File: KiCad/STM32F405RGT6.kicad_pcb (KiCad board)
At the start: 4 copper layers, 101.6 x 101.6 mm, 45 parts, among them J1 USB_C_Receptacle_USB2.0, J201 Conn_02x32_Odd_Even, J202 Conn_02x20_Odd_Even, U1 STM32F405RGTx, U2 AT24CS64-SSHM, Y1 25MHz

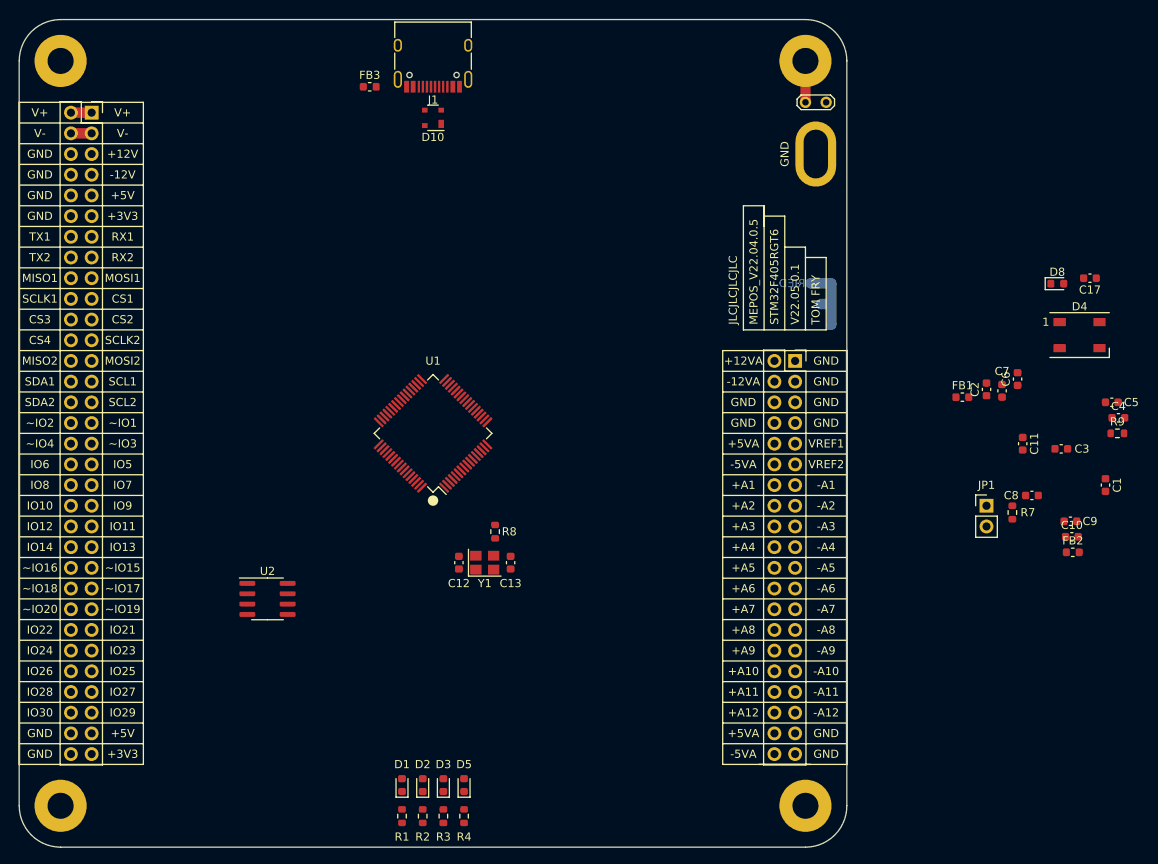
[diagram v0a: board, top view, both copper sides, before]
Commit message: Removed FTDI chip and rearranged pinout
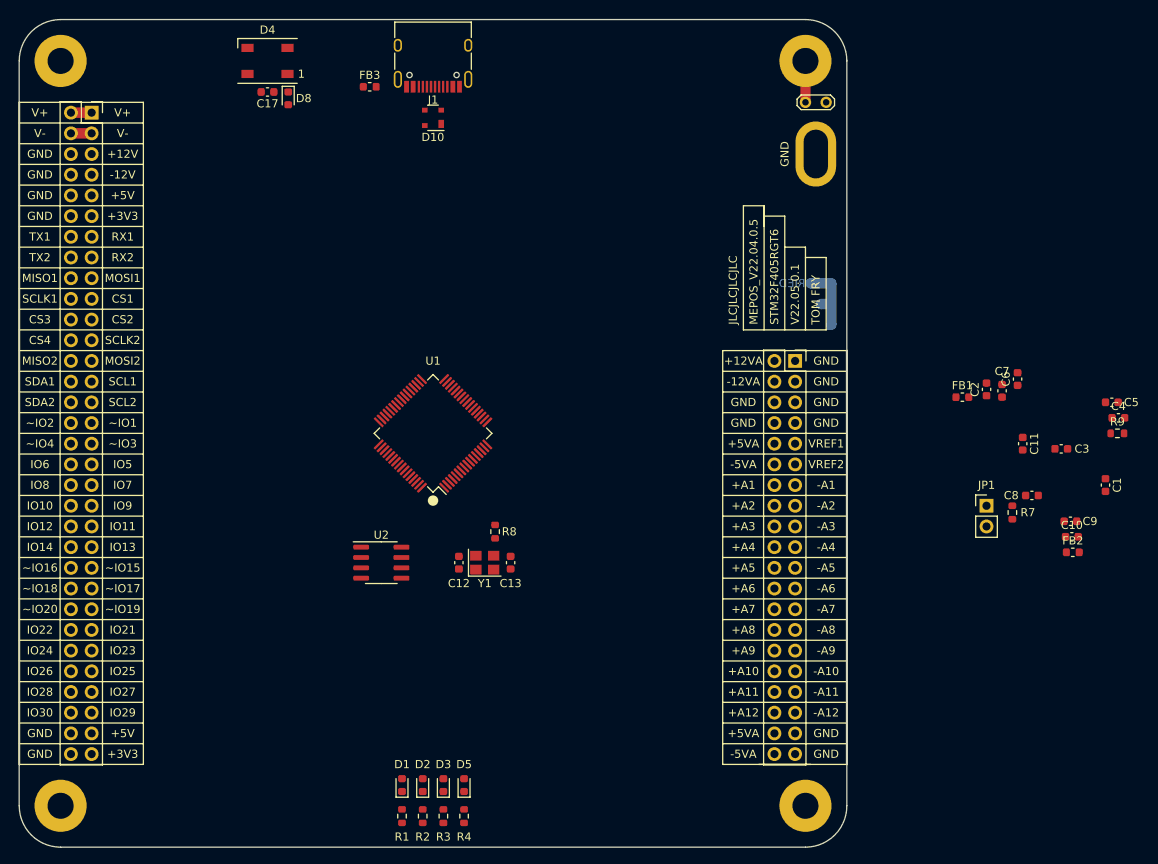
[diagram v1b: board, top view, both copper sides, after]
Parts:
- U2: value AT24CS64-SSHM -> M24C02-RMN
- moved D4 105.2 mm to (124.6, 39.0), turned to 180 degrees
- moved C17 103.5 mm to (124.6, 42.9)
- moved D8 97.1 mm to (127.1, 43.6), turned to -90 degrees
- moved U2 14.7 mm to (138.6, 100.6)

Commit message: Updated Schematic to STM32 software
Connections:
- net FTDI_RST renamed NRST
- U1 pad 2: GPIO10 -> GPIO12
- U1 pad 22: GPIO13 -> GPIO15~
- U1 pad 23: GPIO14 -> GPIO16~
- U1 pad 24: GPIO15~ -> GPIO17~
- U1 pad 25: GPIO16~ -> GPIO18~
- U1 pad 26: GPIO17~ -> GPIO19~
- U1 pad 27: GPIO18~ -> GPIO20~
- U1 pad 3: GPIO11 -> GPIO13
- U1 pad 33: GPIO19~ -> GPIO21
- U1 pad 34: GPIO20~ -> GPIO22
- U1 pad 4: GPIO12 -> GPIO14
- U1 pad 42: FTDI_RX -> TX1
- U1 pad 43: FTDI_TX -> RX1
- U1 pad 44: FTDI_RTS -> GPIO6
- U1 pad 45: FTDI_CTS -> GPIO7
- U1 pad 50: GPIO6 -> GPIO8
- U1 pad 57: GPIO7 -> GPIO9
- U1 pad 58: GPIO8 -> GPIO10
- U1 pad 59: GPIO9 -> GPIO11

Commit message: Updated Schematic and BOM
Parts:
- removed D10: PRTR5V0U2X, Package_TO_SOT_SMD:SOT-143
- added C14: 10uF, Capacitor_SMD:C_0603_1608Metric, F.Cu at (158.8, 46.7)
- added C15: 10uF, Capacitor_SMD:C_0603_1608Metric, F.Cu at (158.8, 44.1)
- added D6: 1N5819WS, Diode_SMD:D_SOD-323, F.Cu at (142.4, 125.0)
- added D7: 1N5819WS, Diode_SMD:D_SOD-323, F.Cu at (155.7, 43.9)
- added D9: 1N5819WS, Diode_SMD:D_SOD-323, F.Cu at (162.7, 49.8)
- added J2: Conn_02x05_Odd_Even, Connector_PinHeader_2.54mm:PinHeader_2x05_P2.54mm_Vertical, F.Cu at (150.0, 129.2)
- added U3: AMS1117-3.3, Package_TO_SOT_SMD:SOT-223-3_TabPin2, F.Cu at (165.2, 44.4)
- added U4: SRV05-4, Package_TO_SOT_SMD:SOT-23-6, F.Cu at (148.7, 46.7)
- moved D1 110.8 mm to (204.6, 37.1)
- moved D2 110.8 mm to (207.2, 37.1)
- moved D3 110.8 mm to (209.7, 37.1)
- moved D5 110.8 mm to (212.2, 37.1)
- moved R1 110.8 mm to (204.6, 40.9)
- moved R2 110.8 mm to (207.2, 40.9)
- moved R3 110.8 mm to (209.7, 40.9)
- moved R4 110.8 mm to (212.2, 40.9)
- moved FB3 15.4 mm to (152.5, 42.9), turned to 180 degrees
- moved J1 0.63 mm to (144.9, 38.8)

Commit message: Updated PCB and Schematic
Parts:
- added C16: 100nF, Capacitor_SMD:C_0603_1608Metric, F.Cu at (167.1, 130.5)
- added SW1: TS-1187A, Button_Switch_SMD:SW_SPST_SKQG_WithStem, F.Cu at (155.1, 130.5)
- added SW2: TS-1187A, Button_Switch_SMD:SW_SPST_SKQG_WithStem, F.Cu at (172.9, 130.5)
- moved R1 114.9 mm to (136.0, 133.2)
- moved R2 114.9 mm to (138.6, 133.2)
- moved R3 114.9 mm to (141.1, 133.2)
- moved R4 114.9 mm to (143.7, 133.2)
- moved D1 113.8 mm to (136.0, 127.9)
- moved D2 113.8 mm to (138.6, 127.9)
- moved D3 113.8 mm to (141.1, 127.9)
- moved D5 113.8 mm to (143.7, 127.9)
- moved C5 97.4 mm to (130.9, 84.8), turned to 90 degrees
- moved C1 88.0 mm to (148.7, 130.5), turned to 90 degrees
- moved C4 83.2 mm to (146.2, 75.2)
- moved C6 82.1 mm to (134.8, 82.9)
- moved C3 79.5 mm to (143.0, 94.9), turned to -90 degrees
- moved R9 79.4 mm to (150.0, 76.5)
- moved R7 77.7 mm to (139.8, 109.5)
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
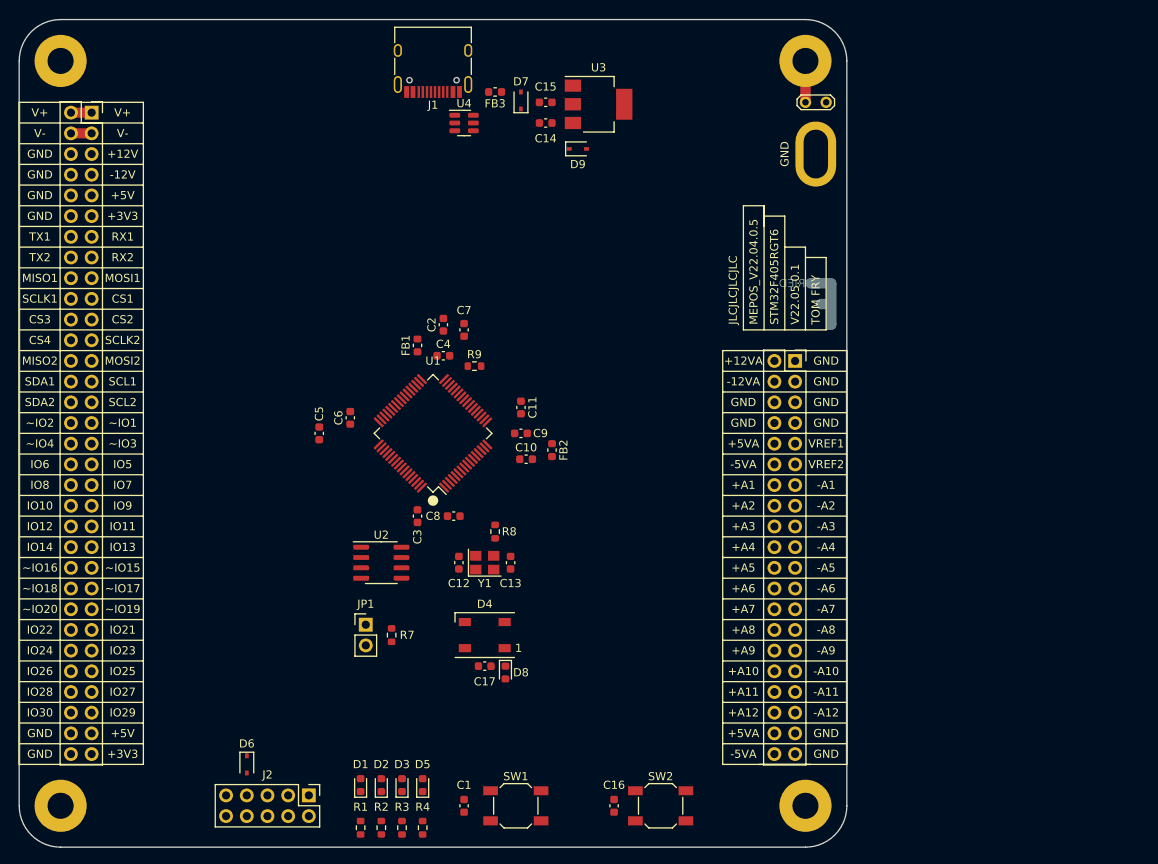
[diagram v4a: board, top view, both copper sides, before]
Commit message: Updated to newer MEPOS Library
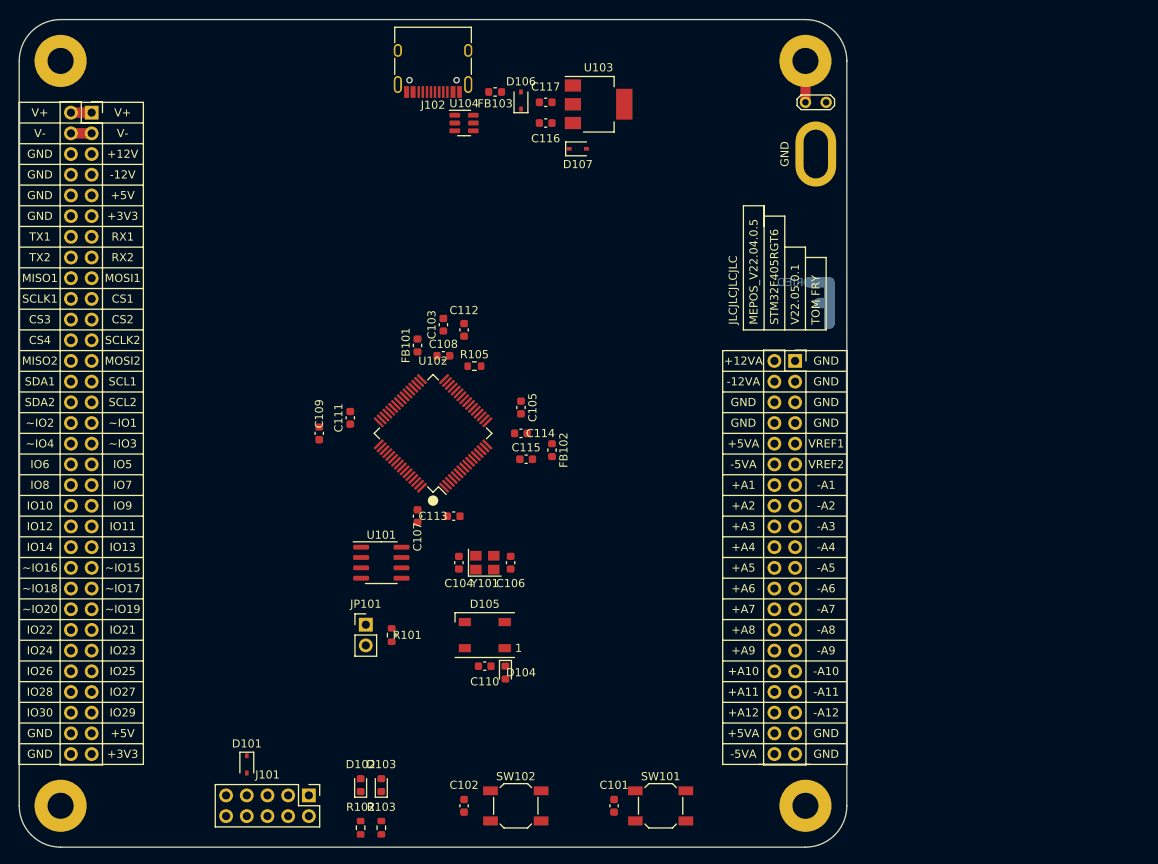
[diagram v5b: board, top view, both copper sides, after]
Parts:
- removed D3, D5: LED_Small, LED_SMD:LED_0603_1608Metric
- removed R3, R4: 1k, Resistor_SMD:R_0603_1608Metric
- removed R8: 470R, Resistor_SMD:R_0603_1608Metric
- added REF**: Logo, MEPOS:Logo, F.Cu at (187.9, 68.8)
- Y101: renamed from Y1; value 25MHz -> 16MHz
- renumbered C16 to C101, C1 to C102, C2 to C103, C12 to C104, C11 to C105, C13 to C106, C3 to C107, C4 to C108, C5 to C109, C17 to C110, C6 to C111, C7 to C112, C8 to C113, C9 to C114, C10 to C115, C14 to C116, C15 to C117, D6 to D101, D1 to D102, D2 to D103, D8 to D104, D4 to D105, D7 to D106, D9 to D107, FB1 to FB101, FB2 to FB102, FB3 to FB103, J2 to J101, J1 to J102, JP1 to JP101, R7 to R101, R1 to R102, R2 to R103, R9 to R105, SW2 to SW101, SW1 to SW102, U2 to U101, U1 to U102, U3 to U103, U4 to U104
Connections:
- net LED_DIN renamed TODO
- C101 pad 1: NRST -> GPIO20~
- C102 pad 1: NRST -> GPIO20~
- C106 pad 1: Net-(C13-Pad1) -> /HSE_OUT
- D102 pad 2: unconnected-(D1-Pad2) -> GPIO20~
- D103 pad 2: unconnected-(D2-Pad2) -> GPIO20~
- D107 pad 1: NRST -> GPIO20~
- FB101 pad 1: NRST -> GPIO20~
- FB102 pad 2: NRST -> +3.3VA
- J101 pad 1: NRST -> GPIO20~
- J102 pad A5: unconnected-(J1-PadA5) -> Net-(J102-PadA5)
- J102 pad B5: unconnected-(J1-PadB5) -> Net-(J102-PadB5)
- J201 pad 11: NRST -> GPIO20~
- J201 pad 63: NRST -> GPIO20~
- JP101 pad 2: NRST -> GPIO20~
- R102 pad 2: unconnected-(R1-Pad2) -> GPIO21
- R103 pad 2: unconnected-(R2-Pad2) -> GPIO22
- SW101 pad 2: NRST -> GPIO20~
- SW102 pad 2: NRST -> GPIO20~
- U102 pad 7: NRST -> GPIO20~
- Y101 pad 3: Net-(C13-Pad1) -> /HSE_OUT
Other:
- board text removed: "LECTRONICS"
- board text removed: "RIED"

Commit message: Updated Schematic and PCB
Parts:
- added JP2: EXT +3V3A, Connector_PinHeader_2.54mm:PinHeader_1x02_P2.54mm_Vertical, F.Cu at (163.3, 83.5)
- added R5: 5k1, Resistor_SMD:R_0603_1608Metric, F.Cu at (147.5, 48.6)
- added R6: 5k1, Resistor_SMD:R_0603_1608Metric, F.Cu at (142.2, 45.4)
- moved D2 3.18 mm to (139.2, 127.9)
- moved D3 3.18 mm to (141.7, 127.9)
- moved R2 3.18 mm to (139.2, 133.2)
- moved R3 3.18 mm to (141.7, 133.2)
- moved C6 3.09 mm to (149.9, 98.1), turned to 0 degrees
- moved C8 2.78 mm to (153.3, 98.1), turned to 0 degrees
- moved U4 0.90 mm to (148.1, 46.0)
- renumbered C116 to C1, C108 to C10, C109 to C11, C111 to C12, C112 to C13, C113 to C14, C114 to C15, C115 to C16, C110 to C17, C117 to C2, C102 to C3, C101 to C4, C103 to C5, C104 to C6, C105 to C7, C106 to C8, C107 to C9, D107 to D1, D102 to D2, D103 to D3, D101 to D4, D104 to D5, D105 to D6, D106 to D7, FB101 to FB1, FB102 to FB2, FB103 to FB3, GND201 to GND1, H201 to H1, H202 to H2, H203 to H3, H204 to H4, J101 to J1, J102 to J2, J201 to J3, J202 to J4, JP101 to JP1, JP201 to JP3, R101 to R1, R102 to R2, R103 to R3, R105 to R4, SW102 to SW1, SW101 to SW2, U103 to U1, U101 to U2, U102 to U3, U104 to U4, Y101 to Y1
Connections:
- C3 pad 1: GPIO20~ -> +3V3
- D1 pad 1: GPIO20~ -> +3V3
- D2 pad 2: GPIO20~ -> +3V3
- D3 pad 2: GPIO20~ -> +3V3
- FB1 pad 1: GPIO20~ -> +3V3
- J1 pad 1: GPIO20~ -> NRST
- J2 pad A5: Net-(J102-PadA5) -> /USB_CC1
- J2 pad B5: Net-(J102-PadB5) -> /USB_CC2
- J3 pad 11: GPIO20~ -> +3V3
- J3 pad 63: GPIO20~ -> +3V3
- JP1 pad 2: GPIO20~ -> +3V3
- SW1 pad 2: GPIO20~ -> +3V3
- U3 pad 7: GPIO20~ -> +3V3
